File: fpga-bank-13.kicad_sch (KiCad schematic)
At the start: 1 part, among them U1 XC7K410T-2FFG900I

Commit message: Bump revision to 1.0.0. Update name on schematic and PCB sheets
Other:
- title: K410T devboard -> Kintex 410T devboard

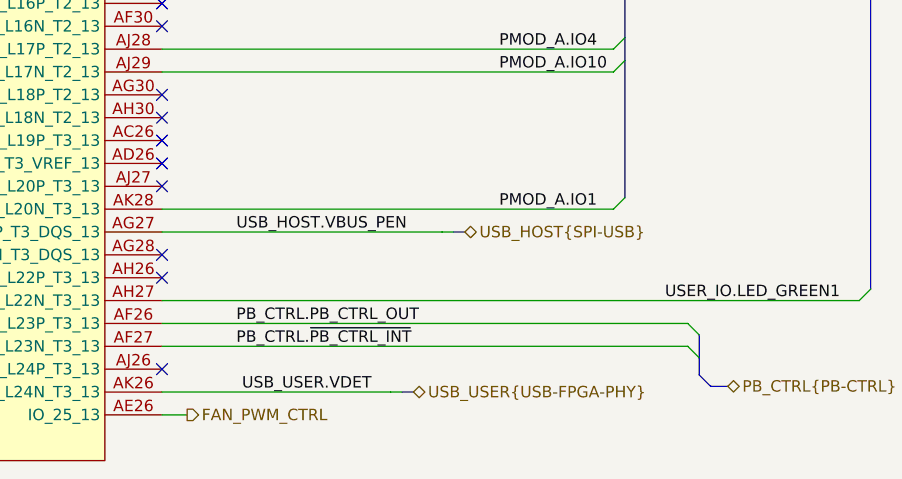
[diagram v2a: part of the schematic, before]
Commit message: Remapped signals and added 0R - related to U33
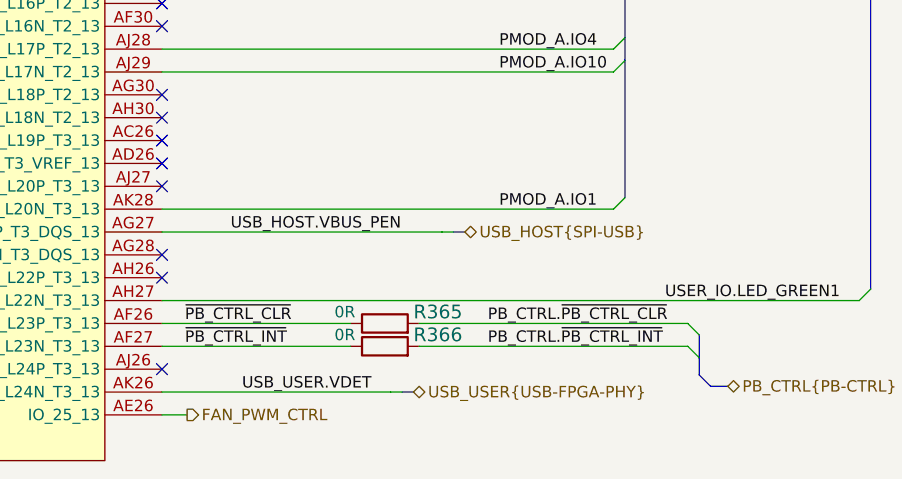
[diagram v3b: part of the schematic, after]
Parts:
- added R365, R366: R_0R_0402, K410T-devboard-footprints:0402-res, symbol K410T-devboard:R_0R_0402
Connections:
- net PB_CTRL.~{PB_CTRL_INT}: now also R366.2; no longer U1.AF27 (IO_L23N_T3_13)
- net PB_CTRL.PB_CTRL_OUT renamed ~{PB_CTRL_CLR}
- net ~{PB_CTRL_CLR}: now also R365.1
- new net PB_CTRL.~{PB_CTRL_CLR}: R365.2
- new net ~{PB_CTRL_INT}: R366.1, U1.AF27 (IO_L23N_T3_13)
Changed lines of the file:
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@@
+    (stroke (width 0) (type default) (color 0 0 0 0))
+  )
+  (wire (pts (xy 172.085 198.12) (xy 201.93 198.12))
     (stroke (width 0) (type default) (color 0 0 0 0))
   )
@@
     (stroke (width 0) (type default) (color 0 0 0 0))
   )
+  (wire (pts (xy 172.085 200.66) (xy 201.93 200.66))
+    (stroke (width 0) (type default) (color 0 0 0 0))
+  )
   (bus (pts (xy 158.75 115.57) (xy 158.75 118.11))
     (stroke (width 0) (type default) (color 0 0 0 0))
@@
     (stroke (width 0) (type default) (color 0 0 0 0))
   )
-  (wire (pts (xy 143.51 200.66) (xy 201.93 200.66))
+  (wire (pts (xy 143.51 200.66) (xy 164.465 200.66))
     (stroke (width 0) (type default) (color 0 0 0 0))
   )
@@
     (stroke (width 0) (type default) (color 0 0 0 0))
   )
-  (wire (pts (xy 143.51 198.12) (xy 201.93 198.12))
+  (wire (pts (xy 143.51 198.12) (xy 164.465 198.12))
     (stroke (width 0) (type default) (color 0 0 0 0))
   )
@@
     )
   )
-  (label "USB_HOST.VBUS_PEN" (at 151.765 187.96 0)
-    (effects (font (size 1.27 1.27)) (justify left bottom))
-  )
   (label "PMOD_A.IO10" (at 180.975 170.18 0)
     (effects (font (size 1.27 1.27)) (justify left bottom))
@@
     (effects (font (size 1.27 1.27)) (justify left bottom))
   )
-  (label "PB_CTRL.PB_CTRL_OUT" (at 151.765 198.12 0)
-    (effects (font (size 1.27 1.27)) (justify left bottom))
-  )
   (label "PMOD_B.IO7" (at 144.78 139.7 0)
     (effects (font (size 1.27 1.27)) (justify left bottom))
   )
+  (label "~{PB_CTRL_INT}" (at 146.05 200.66 0)
+    (effects (font (size 1.27 1.27)) (justify left bottom))
+  )
   (label "PMOD_A.IO7" (at 180.975 111.76 0)
     (effects (font (size 1.27 1.27)) (justify left bottom))
@@
     (effects (font (size 1.27 1.27)) (justify left bottom))
   )
+  (label "PB_CTRL.~{PB_CTRL_CLR}" (at 179.705 198.12 0)
+    (effects (font (size 1.27 1.27)) (justify left bottom))
+  )
   (label "USER_IO.LED_RED" (at 199.39 96.52 0)
     (effects (font (size 1.27 1.27)) (justify left bottom))
@@
     (effects (font (size 1.27 1.27)) (justify left bottom))
   )
-  (label "PB_CTRL.~{PB_CTRL_INT}" (at 151.765 200.66 0)
+  (label "PB_CTRL.~{PB_CTRL_INT}" (at 179.705 200.66 0)
+    (effects (font (size 1.27 1.27)) (justify left bottom))
+  )
+  (label "~{PB_CTRL_CLR}" (at 146.05 198.12 0)
     (effects (font (size 1.27 1.27)) (justify left bottom))
   )
@@
   )
   (label "PMOD_B.IO10" (at 144.78 114.3 0)
+    (effects (font (size 1.27 1.27)) (justify left bottom))
+  )
+  (label "USB_HOST.VBUS_PEN" (at 151.13 187.96 0)
     (effects (font (size 1.27 1.27)) (justify left bottom))
   )
@@
     (effects (font (size 1.27 1.27)) (justify left))
   )
+  (symbol (lib_id "K410T-devboard:R_0R_0402") (at 168.275 198.12 0) (unit 1)
+    (in_bom yes) (on_board yes)
+    (property "Reference" "R365" (id 0) (at 171.45 196.85 0)
+      (effects (font (size 1.524 1.524)) (justify left))
+    )
+    (property "Value" "R_0R_0402" (id 1) (at 168.275 201.93 0)
+      (effects (font (size 1.524 1.524)) hide)
+    )
+    (property "Footprint" "K410T-devboard-footprints:0402-res" (id 2) (at 173.355 193.04 0)
+      (effects (font (size 1.524 1.524)) (justify left) hide)
+    )
+    (property "Datasheet" "" (id 3) (at 168.275 198.12 0)
+      (effects (font (size 1.27 1.27)) hide)
+    )
+    (property "Manufacturer" "PANASONIC" (id 4) (at 173.355 187.96 0)
+      (effects (font (size 1.524 1.524)) (justify left) hide)
+    )
+    (property "MPN" "ERJ2GE0R00X" (id 5) (at 173.355 190.5 0)
+      (effects (font (size 1.524 1.524)) (justify left) hide)
+    )
+    (property "Val" "0R" (id 6) (at 163.83 196.85 0))
+    (pin "1")
+    (pin "2")
+  )
+  (symbol (lib_id "K410T-devboard:R_0R_0402") (at 168.275 200.66 0) (unit 1)
+    (in_bom yes) (on_board yes)
+    (property "Reference" "R366" (id 0) (at 171.45 199.39 0)
+      (effects (font (size 1.524 1.524)) (justify left))
+    )
+    (property "Value" "R_0R_0402" (id 1) (at 168.275 204.47 0)
+      (effects (font (size 1.524 1.524)) hide)
+    )
+    (property "Footprint" "K410T-devboard-footprints:0402-res" (id 2) (at 173.355 195.58 0)
+      (effects (font (size 1.524 1.524)) (justify left) hide)
+    )
+    (property "Datasheet" "" (id 3) (at 168.275 200.66 0)
+      (effects (font (size 1.27 1.27)) hide)
+    )
+    (property "Manufacturer" "PANASONIC" (id 4) (at 173.355 190.5 0)
+      (effects (font (size 1.524 1.524)) (justify left) hide)
+    )
+    (property "MPN" "ERJ2GE0R00X" (id 5) (at 173.355 193.04 0)
+      (effects (font (size 1.524 1.524)) (justify left) hide)
+    )
+    (property "Val" "0R" (id 6) (at 163.83 199.39 0))
+    (pin "1")
+    (pin "2")
+  )
   (symbol (lib_id "K410T-devboard:XC7K410T-2FFG900I") (at 119.38 144.78 0) (unit 12)

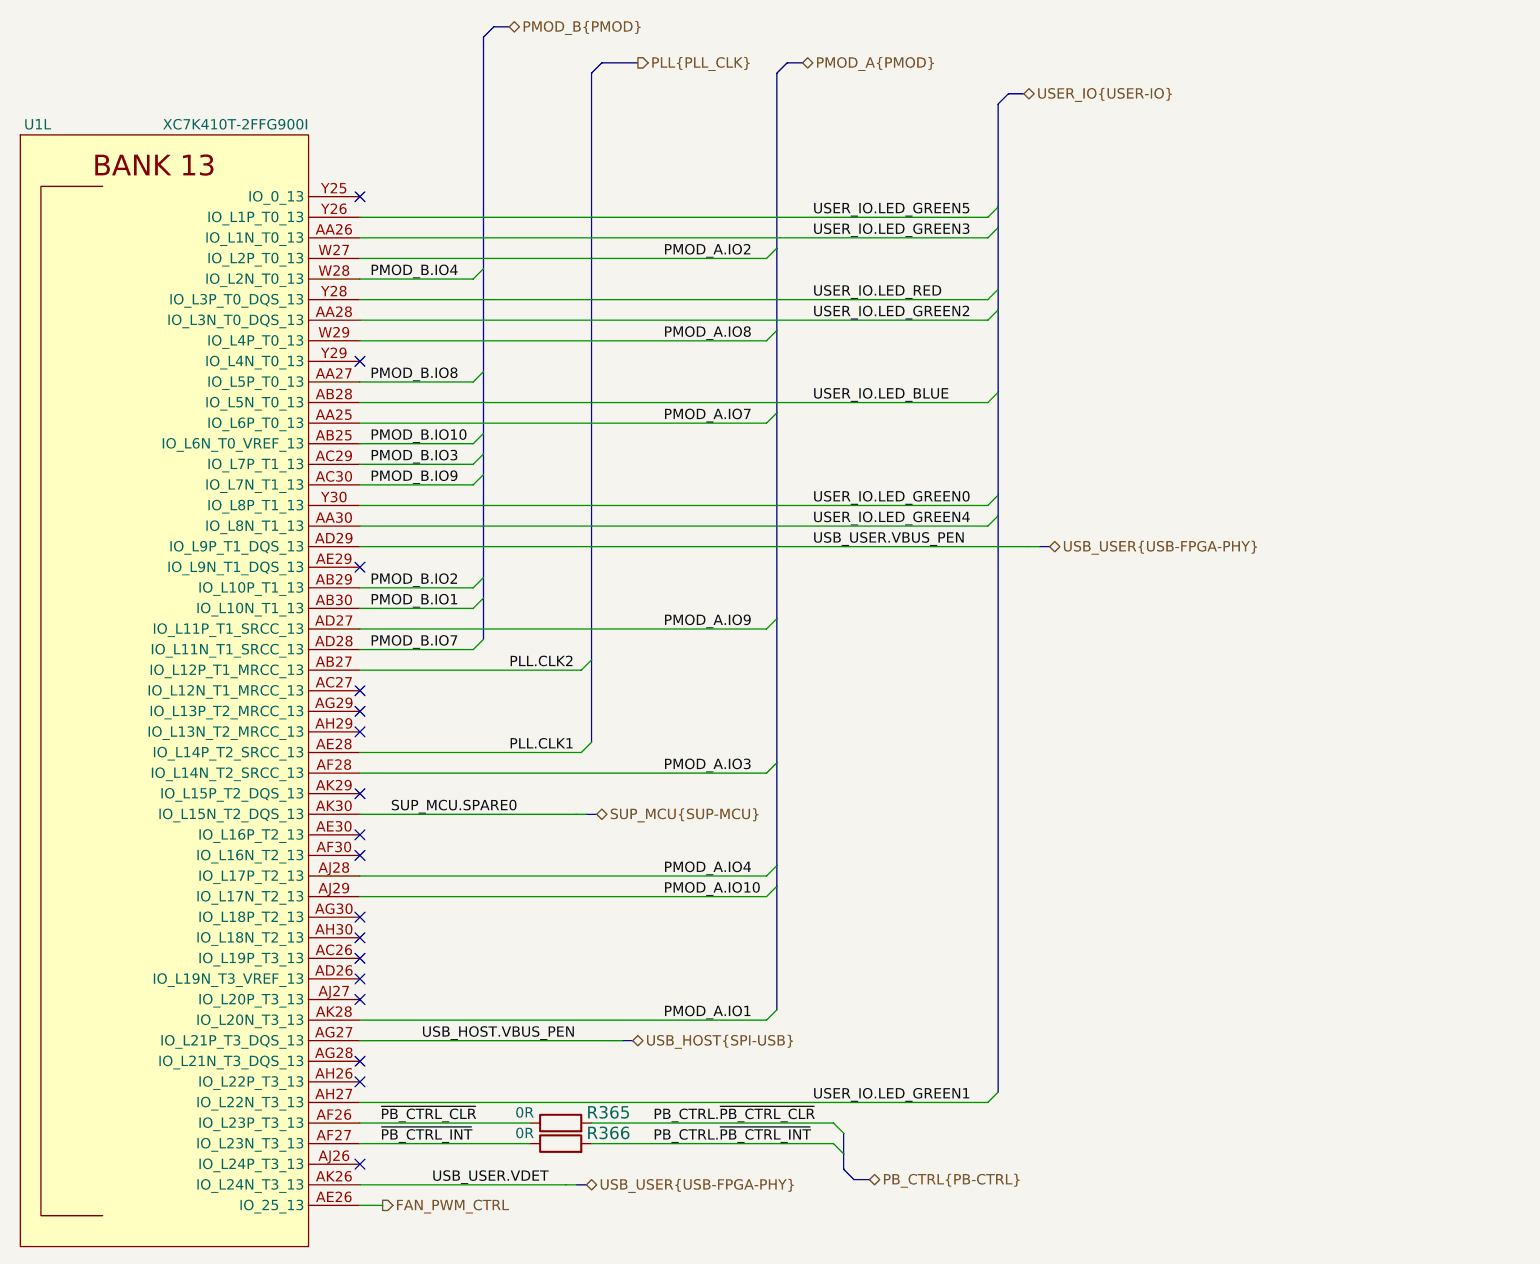
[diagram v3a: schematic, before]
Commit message: Introduce component standardization
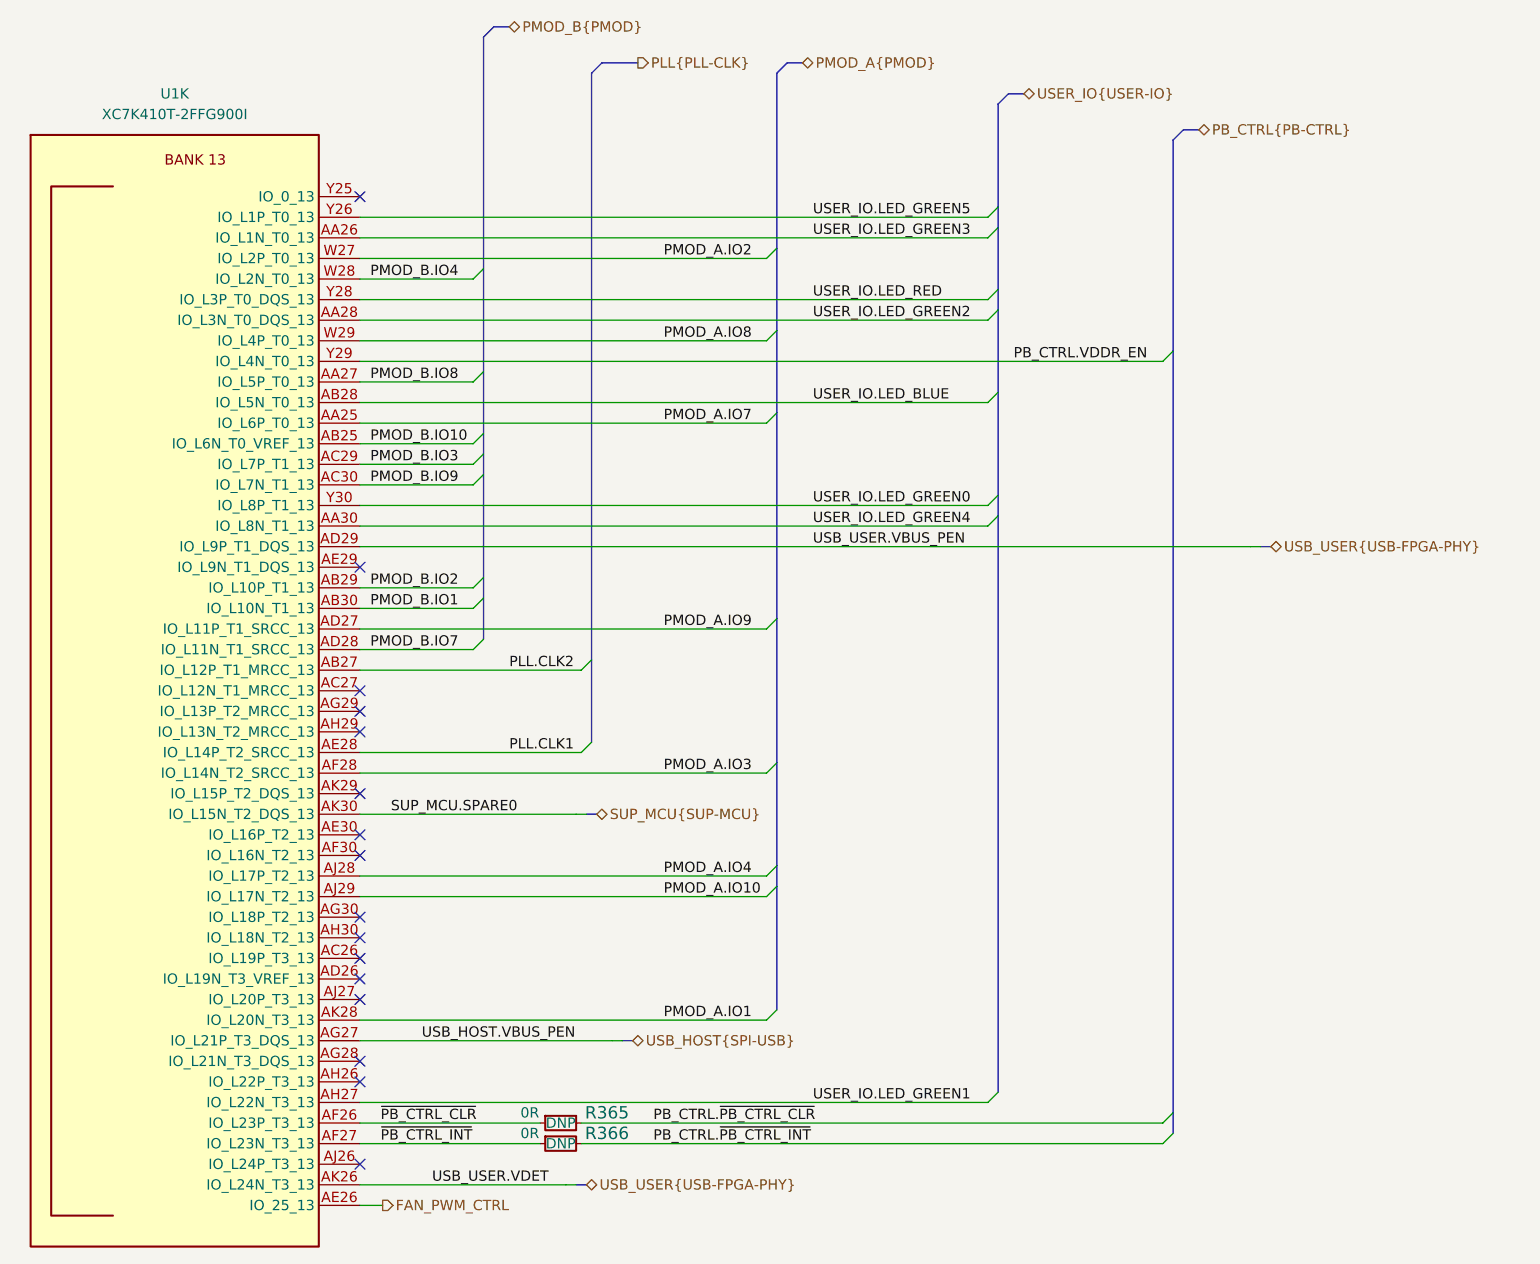
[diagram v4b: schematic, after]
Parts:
- removed U1: XC7K410T-2FFG900I, K410T-devboard-footprints:xc7k410t-2ffg900I, symbol K410T-devboard:XC7K410T-2FFG900I
- added U1: XC7K410T-2FFG900I, K410T-devboard-footprints:xc7k410t-2ffg900I, symbol K410T-devboard:XC7K410T-2FFG900I
- R365, R366: footprint K410T-devboard-footprints:0402-res -> K410T-devboard-footprints:R_0402_1005Metric; Author (none) -> Antmicro; Current (none) -> 1A; DNP (none) -> DNP; License (none) -> Apache-2.0; Manufacturer PANASONIC -> Panasonic
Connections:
- net FAN_PWM_CTRL: now also U1.AE26 (IO_25_13)
- net PLL.CLK1: now also U1.AE28 (IO_L14P_T2_SRCC_13)
- net PLL.CLK2: now also U1.AB27 (IO_L12P_T1_MRCC_13)
- net PMOD_A.IO1: now also U1.AK28 (IO_L20N_T3_13)
- net PMOD_A.IO10: now also U1.AJ29 (IO_L17N_T2_13)
- net PMOD_A.IO2: now also U1.W27 (IO_L2P_T0_13)
- net PMOD_A.IO3: now also U1.AF28 (IO_L14N_T2_SRCC_13)
- net PMOD_A.IO4: now also U1.AJ28 (IO_L17P_T2_13)
- net PMOD_A.IO7: now also U1.AA25 (IO_L6P_T0_13)
- net PMOD_A.IO8: now also U1.W29 (IO_L4P_T0_13)
- net PMOD_A.IO9: now also U1.AD27 (IO_L11P_T1_SRCC_13)
- net PMOD_B.IO1: now also U1.AB30 (IO_L10N_T1_13)
- net PMOD_B.IO10: now also U1.AB25 (IO_L6N_T0_VREF_13)
- net PMOD_B.IO2: now also U1.AB29 (IO_L10P_T1_13)
- net PMOD_B.IO3: now also U1.AC29 (IO_L7P_T1_13)
- net PMOD_B.IO4: now also U1.W28 (IO_L2N_T0_13)
- net PMOD_B.IO7: now also U1.AD28 (IO_L11N_T1_SRCC_13)
- net PMOD_B.IO8: now also U1.AA27 (IO_L5P_T0_13)
- net PMOD_B.IO9: now also U1.AC30 (IO_L7N_T1_13)
- net SUP_MCU.SPARE0: now also U1.AK30 (IO_L15N_T2_DQS_13)
- net USB_HOST.VBUS_PEN: now also U1.AG27 (IO_L21P_T3_DQS_13)
- net USB_USER.VBUS_PEN: now also U1.AD29 (IO_L9P_T1_DQS_13)
- net USB_USER.VDET: now also U1.AK26 (IO_L24N_T3_13)
- net USER_IO.LED_BLUE: now also U1.AB28 (IO_L5N_T0_13)
- net USER_IO.LED_GREEN0: now also U1.Y30 (IO_L8P_T1_13)
- net USER_IO.LED_GREEN1: now also U1.AH27 (IO_L22N_T3_13)
- net USER_IO.LED_GREEN2: now also U1.AA28 (IO_L3N_T0_DQS_13)
- net USER_IO.LED_GREEN3: now also U1.AA26 (IO_L1N_T0_13)
- net USER_IO.LED_GREEN4: now also U1.AA30 (IO_L8N_T1_13)
- net USER_IO.LED_GREEN5: now also U1.Y26 (IO_L1P_T0_13)
- net USER_IO.LED_RED: now also U1.Y28 (IO_L3P_T0_DQS_13)
- net ~{PB_CTRL_CLR}: now also U1.AF26 (IO_L23P_T3_13)
- net ~{PB_CTRL_INT}: now also U1.AF27 (IO_L23N_T3_13)
- new net PB_CTRL.VDDR_EN: U1.Y29 (IO_L4N_T0_13)
- no-connect marks 17 -> 16
